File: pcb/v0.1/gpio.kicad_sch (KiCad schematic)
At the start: 37 parts, among them J7 ComputeModule5-CM5_connector, J8 Micro_SD_molex, J9 AudioJack3, SW1 SW_Push_45deg, U4 PCM5102A, U5 RT9742GGJ5, U6 RT9742GGJ5

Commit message: Assigned all the footprints
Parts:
- J7: footprint (none) -> CM5IO:Raspberry-Pi-5-Compute-Module
- J8: footprint (none) -> CM5IO:SDCARD_MOLEX_503398-1892
- J9: footprint (none) -> TH-1-CC_footprints:STX-3000
- NT1, NT2: footprint (none) -> NetTie:NetTie-2_SMD_Pad0.5mm
- SW1: footprint (none) -> TH-1-CC_footprints:SW_Push_4.5x4.5
- TP1, TP2, TP3, TP6: footprint (none) -> TestPoint:TestPoint_Pad_D1.0mm
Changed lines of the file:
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@@
 			)
 		)
-		(property "Footprint" ""
+		(property "Footprint" "TH-1-CC_footprints:STX-3000"
 			(at 394.97 204.47 0)
 			(hide yes)
@@
 			)
 		)
-		(property "Footprint" ""
+		(property "Footprint" "NetTie:NetTie-2_SMD_Pad0.5mm"
 			(at 215.9 124.46 0)
 			(hide yes)
@@
 			)
 		)
-		(property "Footprint" ""
+		(property "Footprint" "NetTie:NetTie-2_SMD_Pad0.5mm"
 			(at 123.19 93.98 0)
 			(hide yes)
@@
 			)
 		)
-		(property "Footprint" ""
+		(property "Footprint" "TH-1-CC_footprints:SW_Push_4.5x4.5"
 			(at 393.7 44.45 0)
 			(hide yes)
@@
 			)
 		)
-		(property "Footprint" ""
+		(property "Footprint" "TestPoint:TestPoint_Pad_D1.0mm"
 			(at 346.71 106.68 0)
 			(hide yes)
@@
 			)
 		)
-		(property "Footprint" ""
+		(property "Footprint" "TestPoint:TestPoint_Pad_D1.0mm"
 			(at 355.6 149.86 0)
 			(hide yes)
@@
 			)
 		)
-		(property "Footprint" ""
+		(property "Footprint" "CM5IO:Raspberry-Pi-5-Compute-Module"
 			(at 314.96 146.05 0)
 			(hide yes)
@@
 			)
 		)
-		(property "Footprint" ""
+		(property "Footprint" "TestPoint:TestPoint_Pad_D1.0mm"
 			(at 341.63 143.51 0)
 			(hide yes)
@@
 			)
 		)
-		(property "Footprint" ""
+		(property "Footprint" "TestPoint:TestPoint_Pad_D1.0mm"
 			(at 344.17 113.03 0)
 			(hide yes)
@@
 			)
 		)
-		(property "Footprint" ""
+		(property "Footprint" "CM5IO:SDCARD_MOLEX_503398-1892"
 			(at 429.26 63.5 0)
 			(hide yes)

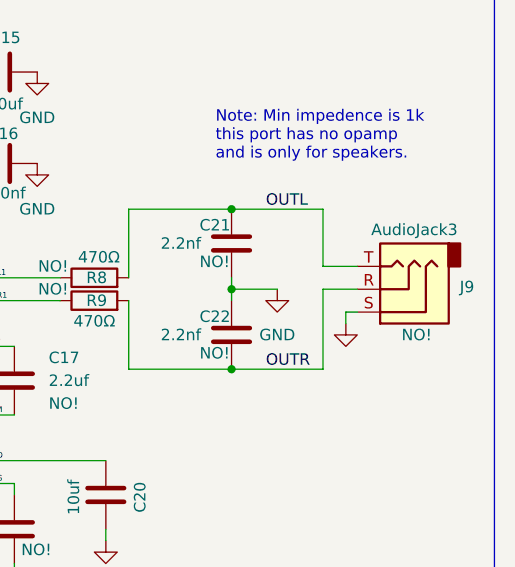
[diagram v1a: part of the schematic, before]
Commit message: Fix footprint numbering issue linkups for pcb import
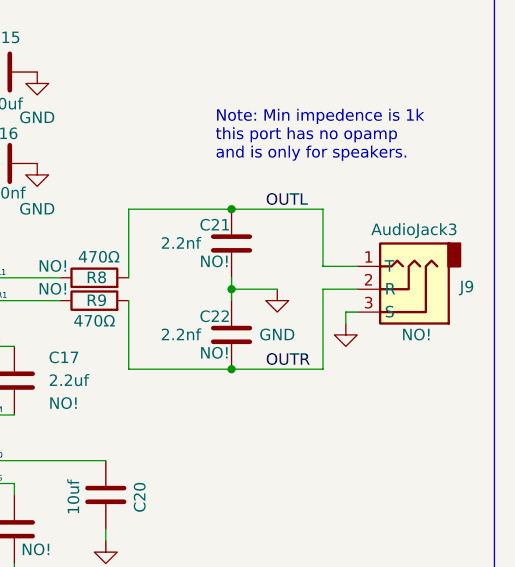
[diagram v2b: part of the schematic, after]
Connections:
- net GND: now also J9.3 (S); no longer J9.S
- net OUTL: now also J9.1 (T); no longer J9.T
- net OUTR: now also J9.2 (R); no longer J9.R
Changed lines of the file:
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@@
 			)
 		)
-		(pin "T"
+		(pin "1"
 		)
-		(pin "S"
+		(pin "2"
 		)
-		(pin "R"
+		(pin "3"
 		)
 		(instances

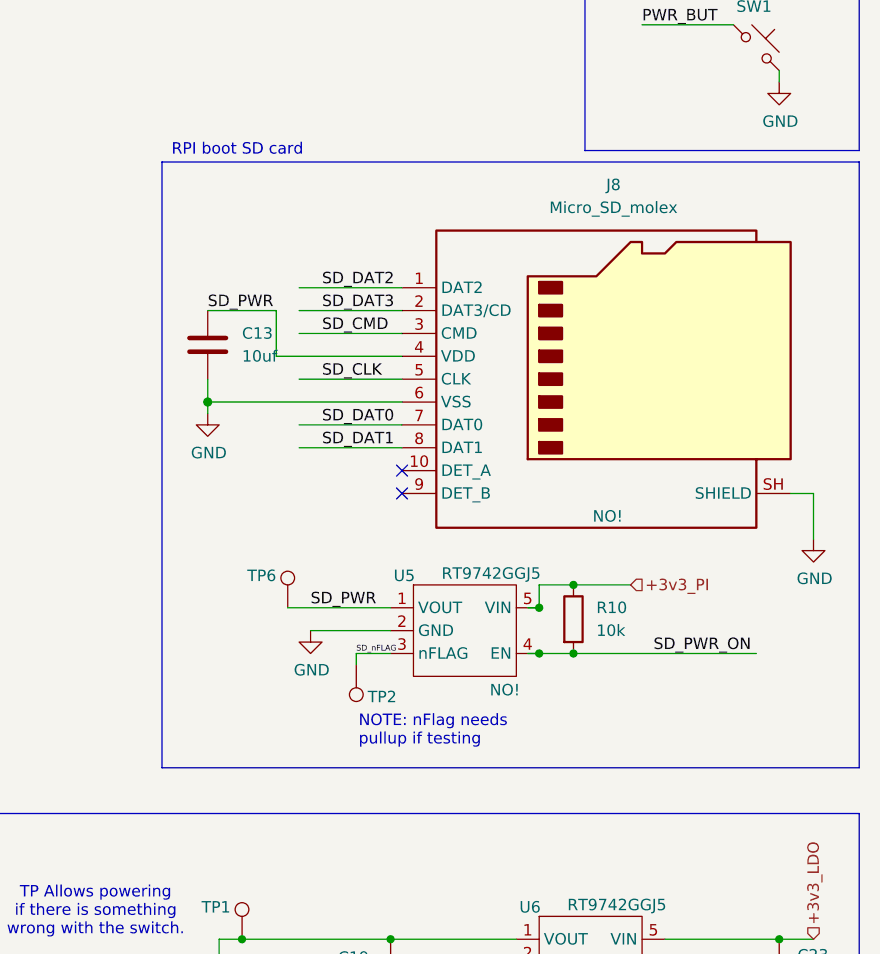
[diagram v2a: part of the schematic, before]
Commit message: A large chunk of the pcb routing + shrinking the board
Did a large chunk of the PCB routing, probably just under half of all
remaining traces. Additionally I shrank the pcb to below 100x100 as it
reduces the price of manufacturing by roughly 4x
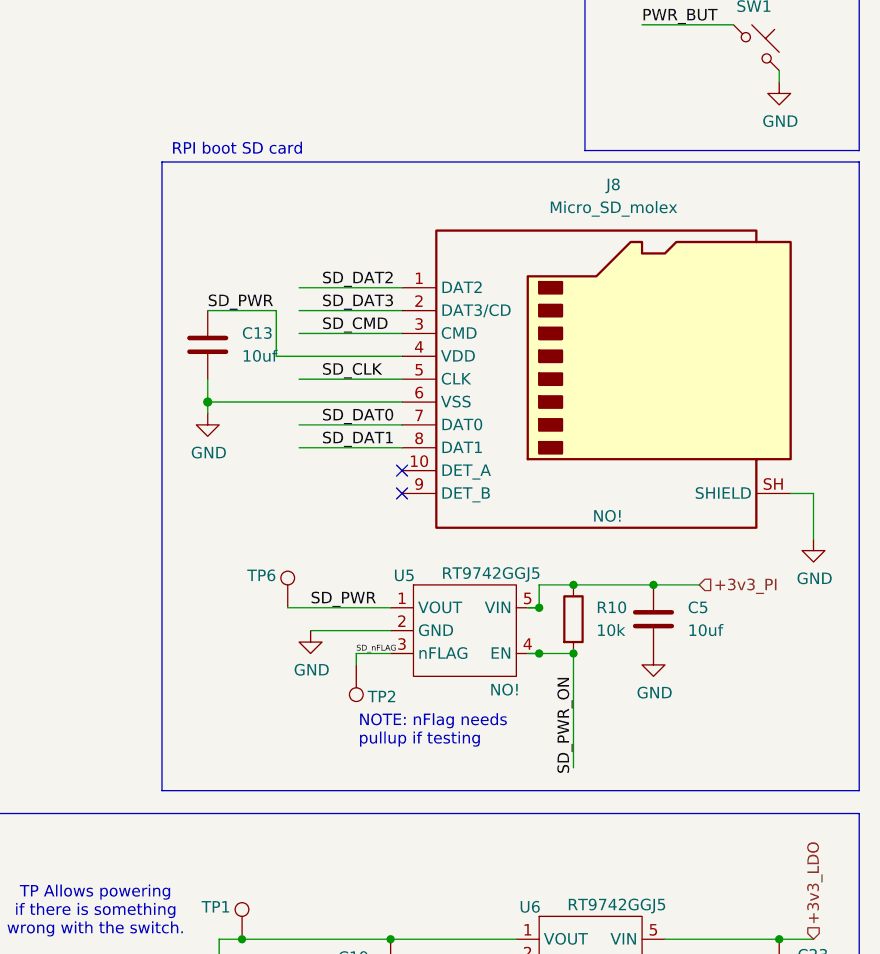
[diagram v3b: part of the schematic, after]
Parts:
- added C5: 10uf, Capacitor_SMD:C_0805_2012Metric, symbol TH-1-CC:C_10uf
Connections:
- net +3v3_PI: now also C5.1
- net GND: now also C5.2
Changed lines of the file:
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@@
 	(rectangle
 		(start 327.66 57.15)
-		(end 405.13 124.46)
+		(end 405.13 127)
 		(stroke
 			(width 0)
@@
 	)
 	(junction
-		(at 373.38 104.14)
+		(at 369.57 111.76)
 		(diameter 0)
 		(color 0 0 0 0)
 	)
 	(junction
-		(at 369.57 111.76)
+		(at 373.38 104.14)
 		(diameter 0)
 		(color 0 0 0 0)
@@
 	)
 	(junction
+		(at 382.27 104.14)
+		(diameter 0)
+		(color 0 0 0 0)
+	)
+	(junction
 		(at 134.62 154.94)
 		(diameter 0)
@@
 	(wire
 		(pts
-			(xy 373.38 111.76) (xy 393.7 111.76)
-		)
-		(stroke
-			(width 0)
-			(type solid)
-		)
-	)
-	(wire
-		(pts
 			(xy 134.62 78.74) (xy 139.7 78.74)
 		)
@@
 	(wire
 		(pts
+			(xy 373.38 111.76) (xy 373.38 124.46)
+		)
+		(stroke
+			(width 0)
+			(type solid)
+		)
+	)
+	(wire
+		(pts
 			(xy 323.85 184.15) (xy 323.85 185.42)
 		)
@@
 	(wire
 		(pts
-			(xy 373.38 104.14) (xy 379.73 104.14)
+			(xy 373.38 104.14) (xy 382.27 104.14)
 		)
 		(stroke
@@
 	(wire
 		(pts
+			(xy 382.27 104.14) (xy 387.35 104.14)
+		)
+		(stroke
+			(width 0)
+			(type solid)
+		)
+	)
+	(wire
+		(pts
 			(xy 132.08 132.08) (xy 139.7 132.08)
 		)
@@
 	)
 	(label "SD_PWR_ON"
-		(at 382.27 111.76 0)
+		(at 373.38 114.3 270)
 		(effects
 			(font
 				(size 1.27 1.27)
 			)
-			(justify left bottom)
+			(justify right bottom)
 		)
 	)
@@
 	(hierarchical_label "+3v3_PI"
 		(shape input)
-		(at 379.73 104.14 0)
+		(at 387.35 104.14 0)
 		(effects
 			(font
@@
 	(symbol
 		(lib_id "power:GND")
+		(at 382.27 111.76 0)
+		(unit 1)
+		(body_style 1)
+		(exclude_from_sim no)
+		(in_bom yes)
+		(on_board yes)
+		(in_pos_files yes)
+		(dnp no)
+		(property "Reference" "#PWR074"
+			(at 382.27 118.11 0)
+			(hide yes)
+			(show_name no)
+			(do_not_autoplace no)
+			(effects
+				(font
+					(size 1.27 1.27)
+				)
+			)
+		)
+		(property "Value" "GND"
+			(at 382.397 116.1542 0)
+			(show_name no)
+			(do_not_autoplace no)
+			(effects
+				(font
+					(size 1.27 1.27)
+				)
+			)
+		)
+		(property "Footprint" ""
+			(at 382.27 111.76 0)
+			(hide yes)
+			(show_name no)
+			(do_not_autoplace no)
+			(effects
+				(font
+					(size 1.27 1.27)
+				)
+			)
+		)
+		(property "Datasheet" ""
+			(at 382.27 111.76 0)
+			(hide yes)
+			(show_name no)
+			(do_not_autoplace no)
+			(effects
+				(font
+					(size 1.27 1.27)
+				)
+			)
+		)
+		(property "Description" "Power symbol creates a global label with name \"GND\" , ground"
+			(at 382.27 111.76 0)
+			(hide yes)
+			(show_name no)
+			(do_not_autoplace no)
+			(effects
+				(font
+					(size 1.27 1.27)
+				)
+			)
+		)
+		(pin "1"
+		)
+		(instances
+			(project "mainboard"
+				(path "/5b8aa782-5c3d-43e7-a869-3bd000015f52/5721f8f0-0440-46b6-aeef-45d87b753dcc"
+					(reference "#PWR074")
+					(unit 1)
+				)
+			)
+		)
+	)
+	(symbol
+		(lib_id "power:GND")
 		(at 396.24 152.4 0)
 		(unit 1)
@@
 					(unit 1)
 				)
+			)
+		)
+	)
+	(symbol
+		(lib_id "TH-1-CC:C_10uf")
+		(at 382.27 107.95 0)
+		(unit 1)
+		(body_style 1)
+		(exclude_from_sim no)
+		(in_bom yes)
+		(on_board yes)
+		(in_pos_files yes)
+		(dnp no)
+		(fields_autoplaced yes)
+		(property "Reference" "C5"
+			(at 386.08 106.68 0)
+			(show_name no)
+			(do_not_autoplace no)
+			(effects
+				(font
+					(size 1.27 1.27)
+				)
+				(justify left)
+			)
+		)
+		(property "Value" "10uf"
+			(at 386.08 109.22 0)
+			(show_name no)
+			(do_not_autoplace no)
+			(effects
+				(font
+					(size 1.27 1.27)
+				)
+				(justify left)
+			)
+		)
+		(property "Footprint" "Capacitor_SMD:C_0805_2012Metric"
+			(at 383.2352 111.76 0)
+			(hide yes)
+			(show_name no)
+			(do_not_autoplace no)
+			(effects
+				(font
+					(size 1.27 1.27)
+				)
+			)
+		)
+		(property "Datasheet" "https://www.lcsc.com/datasheet/C95841.pdf"
+			(at 382.27 107.95 0)
+			(hide yes)
+			(show_name no)
+			(do_not_autoplace no)
+			(effects
+				(font
+					(size 1.27 1.27)
+				)
+			)
+		)
+		(property "Description" "Unpolarized 10uF ±10% 16V Ceramic Capacitor X7R 0805"
+			(at 382.27 107.95 0)
+			(hide yes)
+			(show_name no)
+			(do_not_autoplace no)
+			(effects
+				(font
+					(size 1.27 1.27)
+				)
+			)
+		)
+		(property "Manufacturer" "Samsung Electro-Mechanics"
+			(at 382.27 107.95 0)
+			(hide yes)
+			(show_name no)
+			(do_not_autoplace no)
+			(effects
+				(font
+					(size 1.27 1.27)
+				)
+			)
+		)
+		(property "Mfr. Part no." "CL21B106KOQNNNE"
+			(at 382.27 107.95 0)
+			(hide yes)
+			(show_name no)
+			(do_not_autoplace no)
+			(effects
+				(font
+					(size 1.27 1.27)
+				)
+			)
+		)
+		(property "Distributor LCSC" "https://www.lcsc.com/product-detail/C95841.html?s_z=n_C95841"
+			(at 382.27 107.95 0)
+			(hide yes)
+			(show_name no)
+			(do_not_autoplace no)
+			(effects
+				(font
+					(size 1.27 1.27)
+				)
+			)
+		)
+		(property "LCSC Part no." "C95841"
+			(at 382.27 107.95 0)
+			(hide yes)
+			(show_name no)
+			(do_not_autoplace no)
+			(effects
+				(font
+					(size 1.27 1.27)
+				)
+			)
+		)
+		(pin "1"
+		)
+		(pin "2"
+		)
+		(instances
+			(project "mainboard"
+				(path "/5b8aa782-5c3d-43e7-a869-3bd000015f52/5721f8f0-0440-46b6-aeef-45d87b753dcc"
+					(reference "C5")
+					(unit 1)
+				)

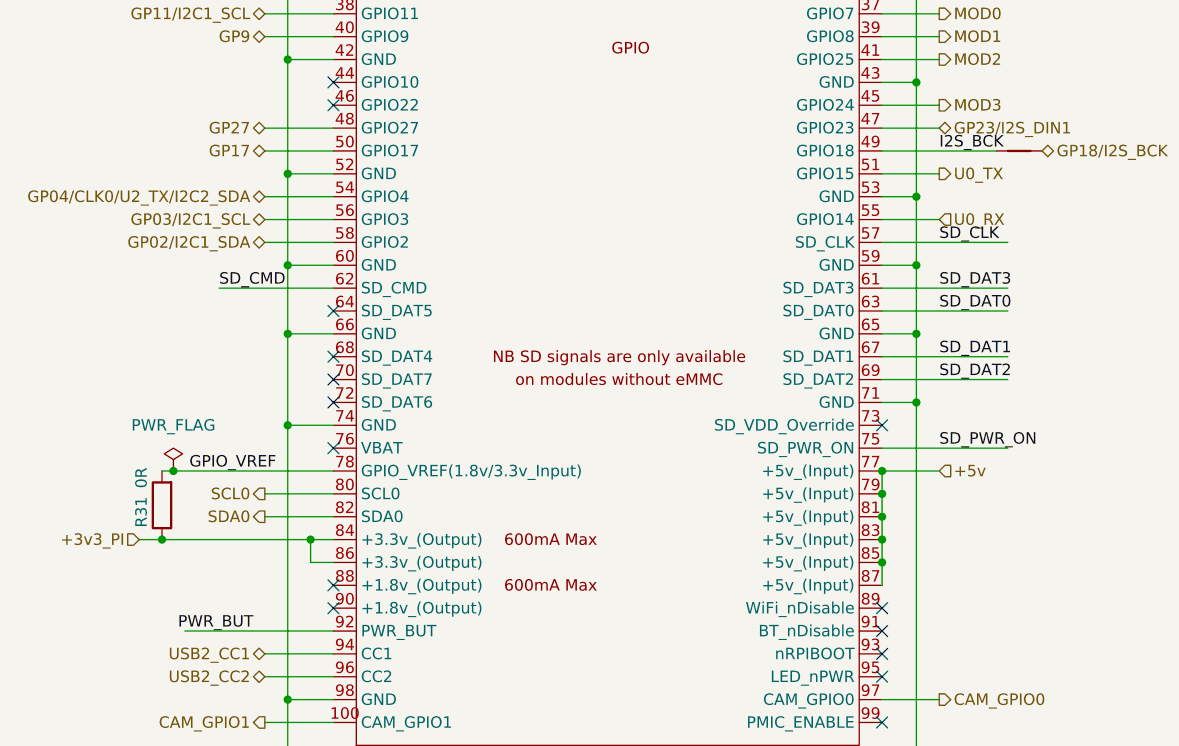
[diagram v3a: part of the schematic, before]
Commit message: Fixing up some DRC errors
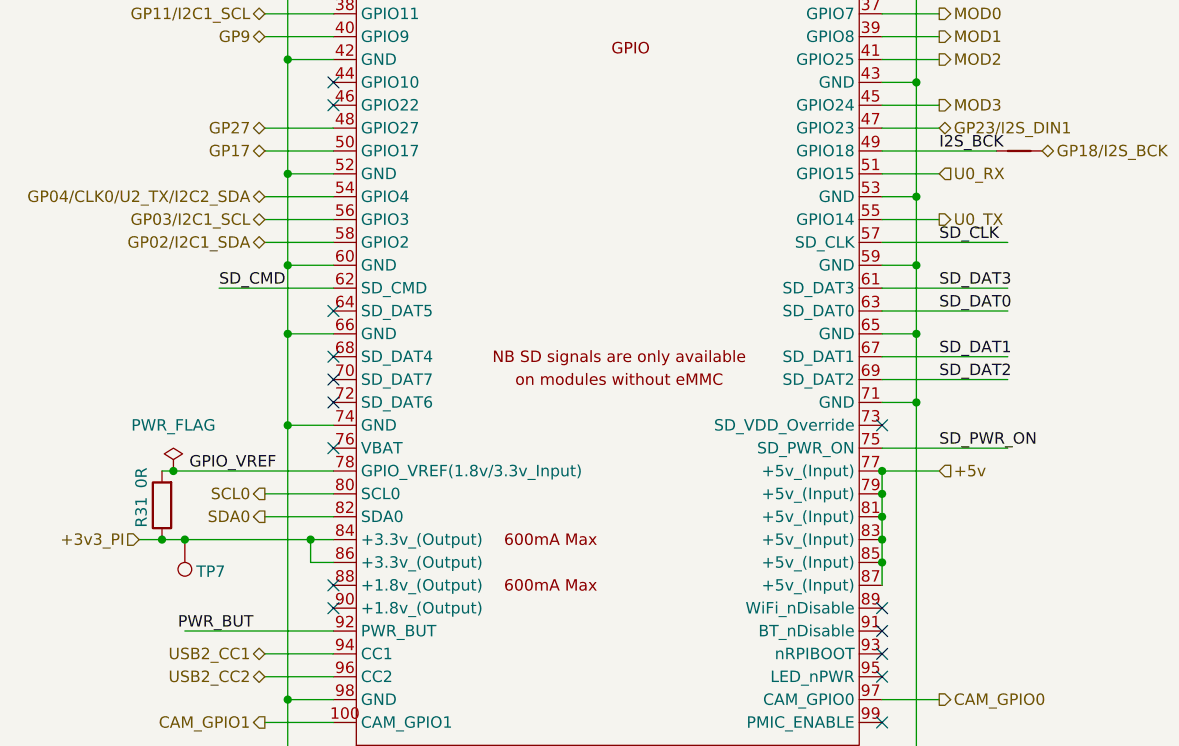
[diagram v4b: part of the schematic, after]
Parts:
- added TP7: TestPoint, TestPoint:TestPoint_Pad_D1.0mm, symbol Connector:TestPoint
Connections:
- net +3v3_PI: now also TP7.1
- net U0_RX: now also J7.51 (GPIO15); no longer J7.55 (GPIO14)
- net U0_TX: now also J7.55 (GPIO14); no longer J7.51 (GPIO15)
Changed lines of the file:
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@@
 	)
 	(junction
+		(at 123.19 167.64)
+		(diameter 0)
+		(color 0 0 0 0)
+	)
+	(junction
 		(at 200.66 167.64)
 		(diameter 0)
@@
 	(wire
 		(pts
-			(xy 381 41.91) (xy 391.16 41.91)
-		)
-		(stroke
-			(width 0)
-			(type default)
-		)
-	)
-	(wire
-		(pts
 			(xy 125.73 93.98) (xy 139.7 93.98)
 		)
@@
 	(wire
 		(pts
-			(xy 120.65 167.64) (xy 137.16 167.64)
+			(xy 120.65 167.64) (xy 123.19 167.64)
 		)
 		(stroke
@@
 	(wire
 		(pts
+			(xy 381 41.91) (xy 391.16 41.91)
+		)
+		(stroke
+			(width 0)
+			(type default)
+		)
+	)
+	(wire
+		(pts
 			(xy 134.62 127) (xy 134.62 114.3)
 		)
@@
 	(wire
 		(pts
+			(xy 123.19 167.64) (xy 137.16 167.64)
+		)
+		(stroke
+			(width 0)
+			(type default)
+		)
+	)
+	(wire
+		(pts
 			(xy 373.38 111.76) (xy 373.38 124.46)
 		)
@@
 	(hierarchical_label "U0_RX"
 		(shape input)
-		(at 207.01 132.08 0)
+		(at 207.01 127 0)
 		(effects
 			(font
@@
 	(hierarchical_label "U0_TX"
 		(shape output)
-		(at 207.01 127 0)
+		(at 207.01 132.08 0)
 		(effects
 			(font
@@
 					(unit 1)
 				)
+			)
+		)
+	)
+	(symbol
+		(lib_id "Connector:TestPoint")
+		(at 123.19 167.64 180)
+		(unit 1)
+		(body_style 1)
+		(exclude_from_sim no)
+		(in_bom yes)
+		(on_board yes)
+		(in_pos_files yes)
+		(dnp no)
+		(property "Reference" "TP7"
+			(at 124.46 171.196 0)
+			(show_name no)
+			(do_not_autoplace no)
+			(effects
+				(font
+					(size 1.27 1.27)
+				)
+				(justify right)
+			)
+		)
+		(property "Value" "TestPoint"
+			(at 125.73 172.2119 0)
+			(hide yes)
+			(show_name no)
+			(do_not_autoplace no)
+			(effects
+				(font
+					(size 1.27 1.27)
+				)
+				(justify right)
+			)
+		)
+		(property "Footprint" "TestPoint:TestPoint_Pad_D1.0mm"
+			(at 118.11 167.64 0)
+			(hide yes)
+			(show_name no)
+			(do_not_autoplace no)
+			(effects
+				(font
+					(size 1.27 1.27)
+				)
+			)
+		)
+		(property "Datasheet" ""
+			(at 118.11 167.64 0)
+			(hide yes)
+			(show_name no)
+			(do_not_autoplace no)
+			(effects
+				(font
+					(size 1.27 1.27)
+				)
+			)
+		)
+		(property "Description" "test point"
+			(at 123.19 167.64 0)
+			(hide yes)
+			(show_name no)
+			(do_not_autoplace no)
+			(effects
+				(font
+					(size 1.27 1.27)
+				)
+			)
+		)
+		(pin "1"
+		)
+		(instances
+			(project "mainboard"
+				(path "/5b8aa782-5c3d-43e7-a869-3bd000015f52/5721f8f0-0440-46b6-aeef-45d87b753dcc"
+					(reference "TP7")
+					(unit 1)
+				)
